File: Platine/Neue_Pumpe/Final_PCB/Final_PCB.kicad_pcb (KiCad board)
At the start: 2 copper layers, 65.1 x 95.3 mm, 146 parts, among them J1 Conn_01x12, J10 Conn_01x02, J2 Conn_01x10, J3 Conn_01x10, J4 Conn_01x10, J5 Conn_01x10, J6 Conn_01x08, J7 Conn_01x06, J8 Conn_01x08, J9 Conn_01x06

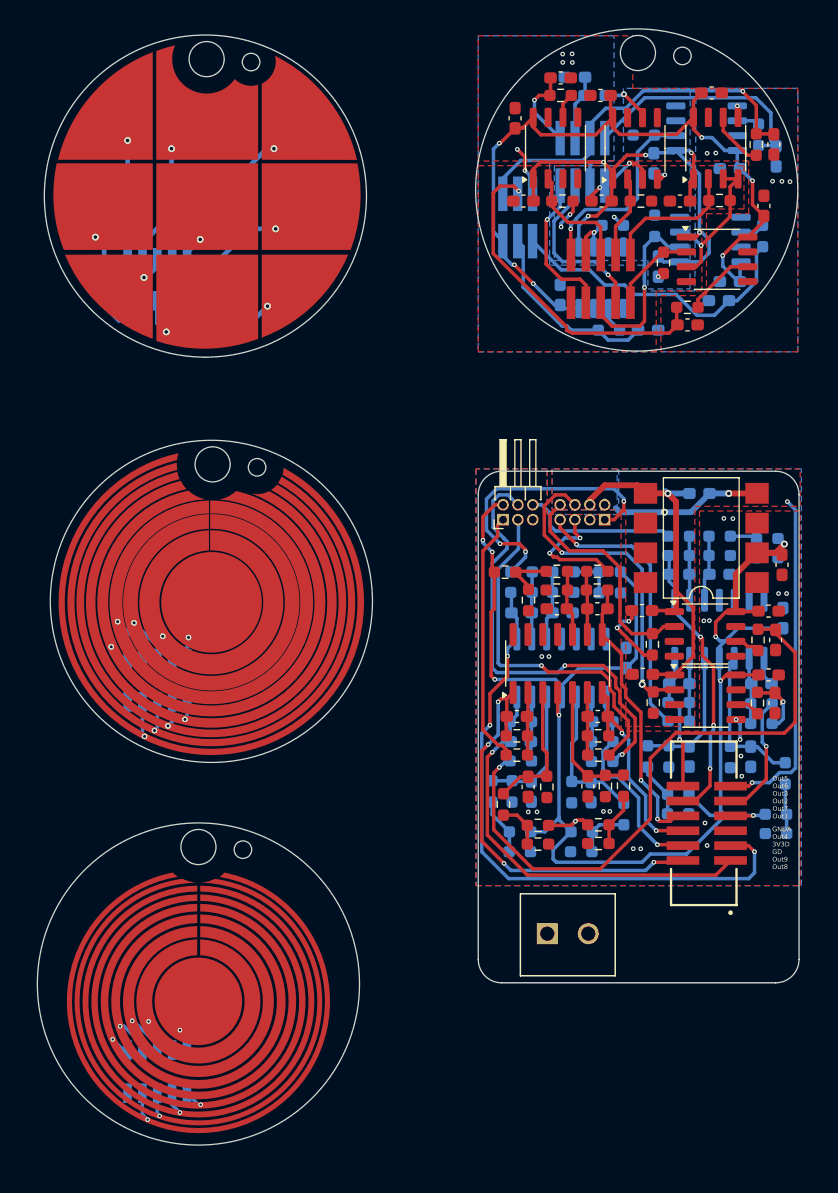
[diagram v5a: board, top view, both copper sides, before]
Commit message: Commit before changing PCB connectors, just in case
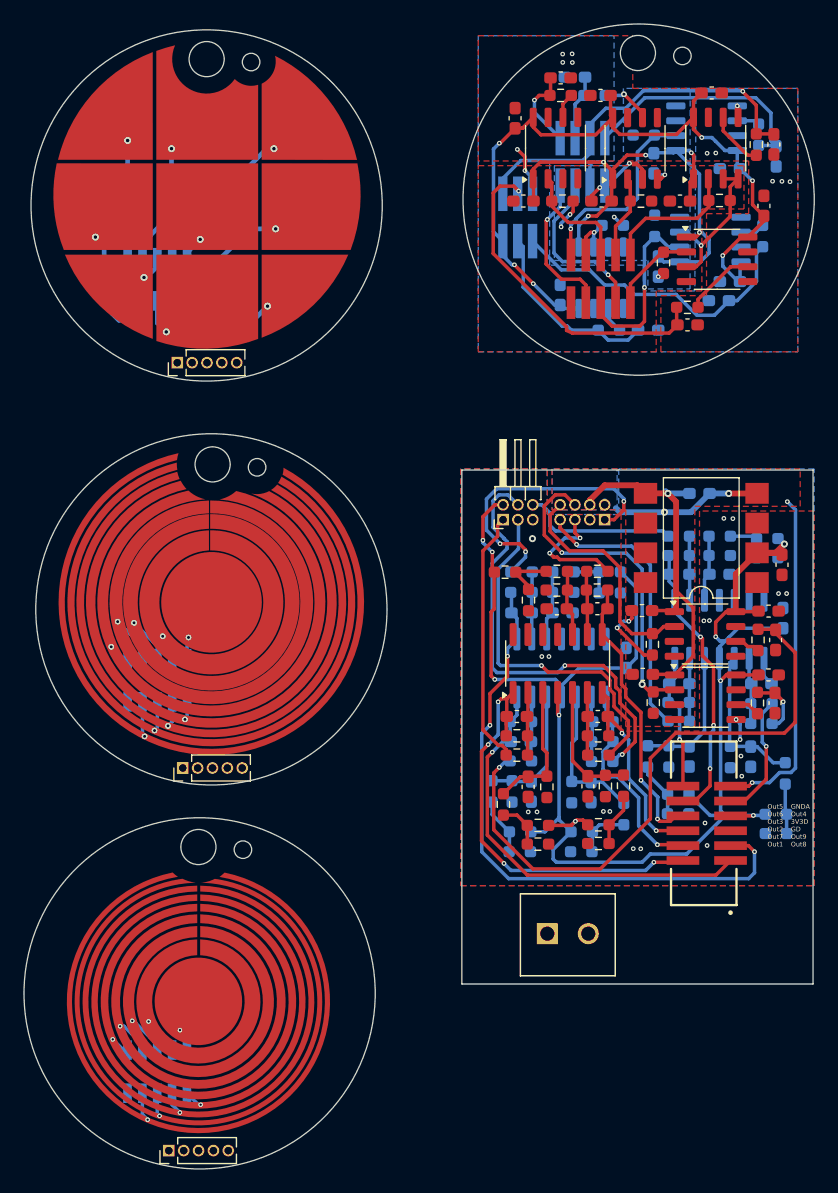
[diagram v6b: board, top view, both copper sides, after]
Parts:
- added J11: Conn_01x05, Connector_PinHeader_1.27mm:PinHeader_1x05_P1.27mm_Vertical, F.Cu at (36.2, 50.9)
- added J12: Conn_01x05, Connector_PinHeader_1.27mm:PinHeader_1x05_P1.27mm_Vertical, F.Cu at (36.7, 85.5)
- added J13: Conn_01x05, Connector_PinHeader_1.27mm:PinHeader_1x05_P1.27mm_Vertical, F.Cu at (35.5, 118.2)
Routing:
- net GNDD: vias 32 -> 33
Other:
- board size 65.1 x 95.3 mm -> 67.5 x 97.8 mm

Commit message: Changed connectors according to stock. Added auxiliar projects for printing each PCB, added component list
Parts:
- removed J6: Conn_01x08, Connector_PinHeader_1.27mm_modified:PinHeader_2x04_P1.27mm_Vertical_SMD
- removed J7: Conn_01x06, Connector_PinHeader_1.27mm:PinHeader_2x03_P1.27mm_Vertical_SMD
- removed J8: Conn_01x08, Connector_PinHeader_1.27mm:PinHeader_2x04_P1.27mm_Horizontal
- removed J9: Conn_01x06, Connector_PinHeader_1.27mm:PinHeader_2x03_P1.27mm_Horizontal
- added J14: Conn_01x14, FTS-107-01-L-D-P:SAMTEC_FTS-107-01-L-D, B.Cu at (68.7, 62.8)
- added J15: Conn_01x14, FTSH-107-01-L-DV-K:SAMTEC_FTSH-107-01-L-DV-K, B.Cu at (69.0, 33.9)
- J10: moved to B.Cu
- R55, R56, R57, R58, R59, R60, R61, R62, R63: value 12.5 -> 281
- moved R68 0.16 mm to (68.8, 28.1)
- turned J10 to 180 degrees
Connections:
- J10 pad 1: unconnected-(J10-Pin_1-Pad1) -> Net-(J10-Pin_1)
- J10 pad 2: unconnected-(J10-Pin_2-Pad2) -> Net-(J10-Pin_1)
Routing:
- net /fil_da5: track 30.9 -> 44.4 mm, vias 2 -> 3
- net /fil_da3: track 16.1 -> 29.2 mm, vias 2 -> 1
- net /fil_da2: track 59.4 -> 71.7 mm, vias 2 -> 3
- net /analog_inp_4: track 57.2 -> 50.2 mm
- net Net-(J10-Pin_1): track 0.00 -> 3.50 mm
- net /fil_da6: track 39.6 -> 43.1 mm
- net /fil_da9: track 45.2 -> 42.8 mm, vias 3 -> 2
- net +3.3VD: track 196.9 -> 199.2 mm, vias 15 -> 13
- net +3.3VA: track 82.8 -> 84.6 mm
- net GNDA: track 75.6 -> 77.0 mm, vias 14 -> 16
- net /analog_inp_8: track 50.3 -> 49.0 mm
- net GNDD: track 7.19 -> 8.18 mm, vias 33 -> 38
- net /fil_da1: track 53.8 -> 53.4 mm, vias 1 -> 3
- net /fil_da7: track 54.3 -> 54.6 mm, vias 2 -> 4
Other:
- outline, holes or cut-outs redrawn
- board text added: "** Grid: The copper wire goes through the hole until the block conector on LP+SC PCB"
- board text added: "GA O4 VD GD O9 O8"
- board text added: "O5 O6 O3 O2 O7 O1"
- board text removed: "** Grid: The tip of the cupper is to be sold to a mini banana connector ** The circle cut must be adapted to the screw-connector width, a cable will be solded behind, which goes to another mini-banana connector that connects finally to the assembly"
- board text removed: "GNDA Out4 3V3D GD Out9 Out8"
- board text removed: "Out5 Out6 Out3 Out2 Out7 Out1"

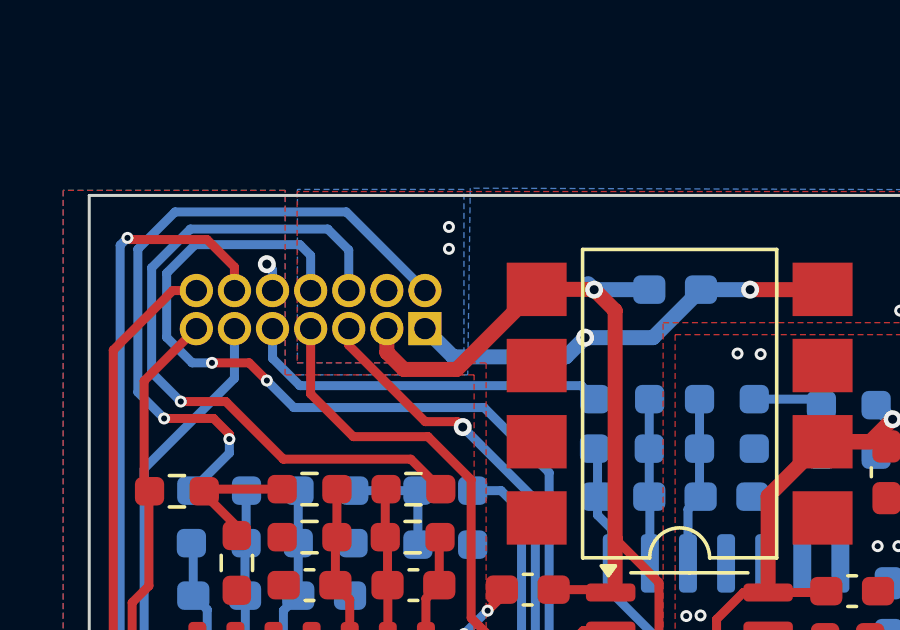
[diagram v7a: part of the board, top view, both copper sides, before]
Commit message: adding some matlab simulations and graphs
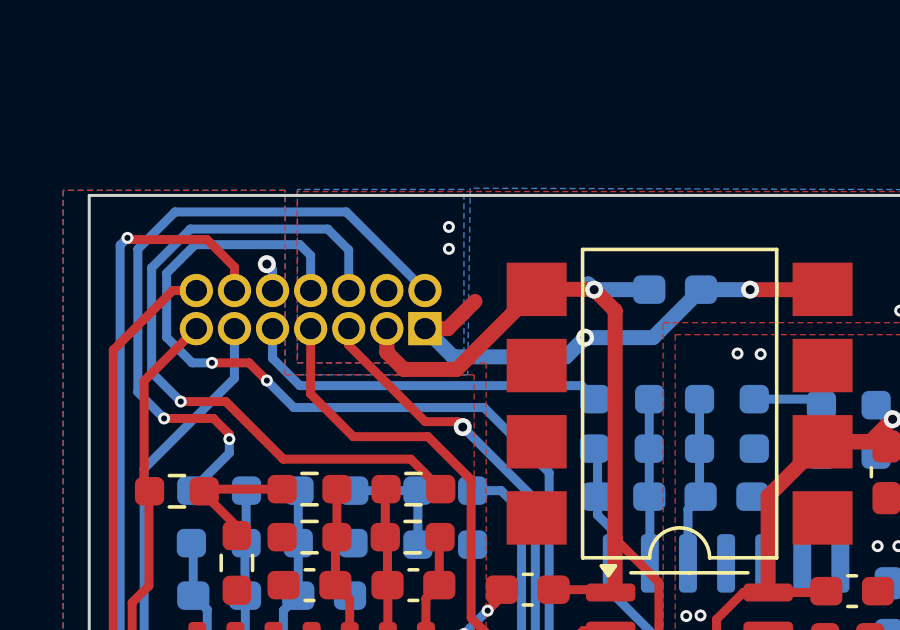
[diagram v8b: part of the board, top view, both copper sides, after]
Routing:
- net GNDA: track 77.0 -> 79.1 mm
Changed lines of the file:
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@@
+	)
+	(segment
+		(start 73.22 63.4)
+		(end 74.13 62.49)
+		(width 0.5)
+		(layer "F.Cu")
+		(net 31)
 	)
 	(segment
@@
 		(layer "F.Cu")
 		(net 31)
+	)
+	(segment
+		(start 72.46 63.4)
+		(end 73.22 63.4)
+		(width 0.5)
+		(layer "F.Cu")
+		(net 31)
